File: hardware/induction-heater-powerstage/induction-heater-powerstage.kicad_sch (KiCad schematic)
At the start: 17 parts, among them IC1 MAX17601ASA+, J2 Screw_Terminal_01x02, J3 Screw_Terminal_01x01, J4 Screw_Terminal_01x01, J5 Screw_Terminal_01x01, J6 Screw_Terminal_01x01, J7 RJ12, Q1 NTH4L040N120M3S, Q3 NTH4L040N120M3S

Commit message: Fixed the mosfet driver grounds
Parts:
- removed JP1: SolderJumper_2_Open, Jumper:SolderJumper-2_P1.3mm_Open_TrianglePad1.0x1.5mm, symbol Jumper:SolderJumper_2_Open
- added NT1: NetTie_2, NetTie:NetTie-2_SMD_Pad2.0mm, symbol Device:NetTie_2
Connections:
- net GND: now also C1.2, J7.3, J7.5, NT1.2
- net GND2: now also NT1.1; no longer C1.2, J7.3, J7.5
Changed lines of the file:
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@@
 (kicad_sch (version 20230121) (generator eeschema)
   (paper "A4")
+  (junction (at 185.42 104.14) (diameter 0) (color 0 0 0 0)
+  )
   (junction (at 101.6 114.3) (diameter 0) (color 0 0 0 0)
   )
-  (junction (at 190.5 104.14) (diameter 0) (color 0 0 0 0)
-  )
   (junction (at 101.6 82.55) (diameter 0) (color 0 0 0 0)
   )
@@
   (junction (at 101.6 97.79) (diameter 0) (color 0 0 0 0)
   )
-  (junction (at 190.5 109.22) (diameter 0) (color 0 0 0 0)
+  (junction (at 196.85 104.14) (diameter 0) (color 0 0 0 0)
   )
   (junction (at 180.34 76.2) (diameter 0) (color 0 0 0 0)
@@
     (stroke (width 0) (type default))
   )
-  (wire (pts (xy 200.66 99.06) (xy 190.5 99.06))
+  (wire (pts (xy 200.66 99.06) (xy 196.85 99.06))
     (stroke (width 0) (type default))
   )
@@
     (stroke (width 0) (type default))
   )
-  (wire (pts (xy 196.85 109.22) (xy 190.5 109.22))
-    (stroke (width 0) (type default))
-  )
   (wire (pts (xy 133.35 130.81) (xy 133.35 139.7))
     (stroke (width 0) (type default))
@@
     (stroke (width 0) (type default))
   )
+  (wire (pts (xy 196.85 104.14) (xy 196.85 114.3))
+    (stroke (width 0) (type default))
+  )
   (wire (pts (xy 154.94 101.6) (xy 142.24 101.6))
     (stroke (width 0) (type default))
@@
     (stroke (width 0) (type default))
   )
+  (wire (pts (xy 193.04 104.14) (xy 196.85 104.14))
+    (stroke (width 0) (type default))
+  )
   (wire (pts (xy 125.73 130.81) (xy 133.35 130.81))
     (stroke (width 0) (type default))
@@
     (stroke (width 0) (type default))
   )
-  (wire (pts (xy 196.85 118.11) (xy 196.85 119.38))
-    (stroke (width 0) (type default))
-  )
   (wire (pts (xy 95.25 100.33) (xy 95.25 104.14))
     (stroke (width 0) (type default))
@@
     (stroke (width 0) (type default))
   )
-  (wire (pts (xy 196.85 110.49) (xy 196.85 109.22))
-    (stroke (width 0) (type default))
-  )
   (wire (pts (xy 133.35 91.44) (xy 133.35 101.6))
     (stroke (width 0) (type default))
   )
-  (wire (pts (xy 190.5 99.06) (xy 190.5 104.14))
+  (wire (pts (xy 196.85 99.06) (xy 196.85 104.14))
     (stroke (width 0) (type default))
   )
@@
     (stroke (width 0) (type default))
   )
-  (wire (pts (xy 190.5 104.14) (xy 190.5 109.22))
-    (stroke (width 0) (type default))
-  )
   (wire (pts (xy 154.94 106.68) (xy 142.24 106.68))
     (stroke (width 0) (type default))
@@
     (stroke (width 0) (type default))
   )
-  (wire (pts (xy 182.88 104.14) (xy 190.5 104.14))
+  (wire (pts (xy 182.88 104.14) (xy 185.42 104.14))
     (stroke (width 0) (type default))
   )
@@
     (stroke (width 0) (type default))
   )
+  (wire (pts (xy 185.42 104.14) (xy 185.42 114.3))
+    (stroke (width 0) (type default))
+  )
   (wire (pts (xy 125.73 91.44) (xy 133.35 91.44))
     (stroke (width 0) (type default))
@@
     (stroke (width 0) (type default))
   )
-  (wire (pts (xy 190.5 109.22) (xy 190.5 119.38))
-    (stroke (width 0) (type default))
-  )
   (wire (pts (xy 175.26 76.2) (xy 180.34 76.2))
     (stroke (width 0) (type default))
   )
+  (wire (pts (xy 185.42 104.14) (xy 187.96 104.14))
+    (stroke (width 0) (type default))
+  )
+  (wire (pts (xy 196.85 104.14) (xy 200.66 104.14))
+    (stroke (width 0) (type default))
+  )
   (wire (pts (xy 101.6 109.22) (xy 101.6 114.3))
     (stroke (width 0) (type default))
@@
   )
   (wire (pts (xy 101.6 114.3) (xy 118.11 114.3))
-    (stroke (width 0) (type default))
-  )
-  (wire (pts (xy 190.5 104.14) (xy 200.66 104.14))
     (stroke (width 0) (type default))
   )
@@
     )
   )
-  (symbol (lib_id "power:GND2") (at 190.5 119.38 0) (unit 1)
-    (in_bom yes) (on_board yes) (dnp no) (fields_autoplaced)
-    (property "Reference" "#PWR07" (at 190.5 125.73 0)
-      (effects (font (size 1.27 1.27)) hide)
-    )
-    (property "Value" "GND2" (at 190.5 124.46 0)
-      (effects (font (size 1.27 1.27)))
-    )
-    (property "Footprint" "" (at 190.5 119.38 0)
-      (effects (font (size 1.27 1.27)) hide)
-    )
-    (property "Datasheet" "" (at 190.5 119.38 0)
+  (symbol (lib_id "power:GND2") (at 185.42 114.3 0) (unit 1)
+    (in_bom yes) (on_board yes) (dnp no) (fields_autoplaced)
+    (property "Reference" "#PWR07" (at 185.42 120.65 0)
+      (effects (font (size 1.27 1.27)) hide)
+    )
+    (property "Value" "GND2" (at 185.42 119.38 0)
+      (effects (font (size 1.27 1.27)))
+    )
+    (property "Footprint" "" (at 185.42 114.3 0)
+      (effects (font (size 1.27 1.27)) hide)
+    )
+    (property "Datasheet" "" (at 185.42 114.3 0)
       (effects (font (size 1.27 1.27)) hide)
     )
@@
         (path "/cd13bc0f-8ba2-41f2-9e37-856c295399b9"
           (reference "L1") (unit 1)
+        )
+      )
+    )
+  )
+  (symbol (lib_id "power:GND") (at 196.85 114.3 0) (unit 1)
+    (in_bom yes) (on_board yes) (dnp no) (fields_autoplaced)
+    (property "Reference" "#PWR010" (at 196.85 120.65 0)
+      (effects (font (size 1.27 1.27)) hide)
+    )
+    (property "Value" "GND" (at 196.85 119.38 0)
+      (effects (font (size 1.27 1.27)))
+    )
+    (property "Footprint" "" (at 196.85 114.3 0)
+      (effects (font (size 1.27 1.27)) hide)
+    )
+    (property "Datasheet" "" (at 196.85 114.3 0)
+      (effects (font (size 1.27 1.27)) hide)
+    )
+    (pin "1")
+    (instances
+      (project "induction-heater-powerstage"
+        (path "/27d95e22-9cd6-4512-b5aa-6a1ddb34ce7c"
+          (reference "#PWR010") (unit 1)
         )
       )
@@
         (path "/27d95e22-9cd6-4512-b5aa-6a1ddb34ce7c"
           (reference "#PWR03") (unit 1)
-        )
-      )
-    )
-  )
-  (symbol (lib_id "power:GND") (at 196.85 119.38 0) (unit 1)
-    (in_bom yes) (on_board yes) (dnp no) (fields_autoplaced)
-    (property "Reference" "#PWR09" (at 196.85 125.73 0)
-      (effects (font (size 1.27 1.27)) hide)
-    )
-    (property "Value" "GND" (at 196.85 124.46 0)
-      (effects (font (size 1.27 1.27)))
-    )
-    (property "Footprint" "" (at 196.85 119.38 0)
-      (effects (font (size 1.27 1.27)) hide)
-    )
-    (property "Datasheet" "" (at 196.85 119.38 0)
-      (effects (font (size 1.27 1.27)) hide)
-    )
-    (pin "1")
-    (instances
-      (project "induction-heater-powerstage"
-        (path "/27d95e22-9cd6-4512-b5aa-6a1ddb34ce7c"
-          (reference "#PWR09") (unit 1)
-        )
-      )
-    )
-  )
-  (symbol (lib_id "power:GND2") (at 152.4 119.38 0) (unit 1)
-    (in_bom yes) (on_board yes) (dnp no) (fields_autoplaced)
-    (property "Reference" "#PWR04" (at 152.4 125.73 0)
-      (effects (font (size 1.27 1.27)) hide)
-    )
-    (property "Value" "GND2" (at 152.4 124.46 0)
-      (effects (font (size 1.27 1.27)))
-    )
-    (property "Footprint" "" (at 152.4 119.38 0)
-      (effects (font (size 1.27 1.27)) hide)
-    )
-    (property "Datasheet" "" (at 152.4 119.38 0)
-      (effects (font (size 1.27 1.27)) hide)
-    )
-    (pin "1")
-    (instances
-      (project "induction-heater-powerstage"
-        (path "/27d95e22-9cd6-4512-b5aa-6a1ddb34ce7c"
-          (reference "#PWR04") (unit 1)
         )
       )
@@
     )
   )
+  (symbol (lib_id "power:GND") (at 152.4 119.38 0) (unit 1)
+    (in_bom yes) (on_board yes) (dnp no) (fields_autoplaced)
+    (property "Reference" "#PWR04" (at 152.4 125.73 0)
+      (effects (font (size 1.27 1.27)) hide)
+    )
+    (property "Value" "GND" (at 152.4 124.46 0)
+      (effects (font (size 1.27 1.27)))
+    )
+    (property "Footprint" "" (at 152.4 119.38 0)
+      (effects (font (size 1.27 1.27)) hide)
+    )
+    (property "Datasheet" "" (at 152.4 119.38 0)
+      (effects (font (size 1.27 1.27)) hide)
+    )
+    (pin "1")
+    (instances
+      (project "induction-heater-powerstage"
+        (path "/27d95e22-9cd6-4512-b5aa-6a1ddb34ce7c"
+          (reference "#PWR04") (unit 1)
+        )
+      )
+    )
+  )
   (symbol (lib_id "Connector:Screw_Terminal_01x01") (at 118.11 120.65 270) (unit 1)
     (in_bom yes) (on_board yes) (dnp no) (fields_autoplaced)
@@
     )
   )
-  (symbol (lib_id "Jumper:SolderJumper_2_Open") (at 196.85 114.3 90) (unit 1)
-    (in_bom yes) (on_board yes) (dnp no) (fields_autoplaced)
-    (property "Reference" "JP1" (at 199.39 113.03 90)
-      (effects (font (size 1.27 1.27)) (justify right))
-    )
-    (property "Value" "SolderJumper_2_Open" (at 199.39 115.57 90)
-      (effects (font (size 1.27 1.27)) (justify right))
-    )
-    (property "Footprint" "Jumper:SolderJumper-2_P1.3mm_Open_TrianglePad1.0x1.5mm" (at 196.85 114.3 0)
-      (effects (font (size 1.27 1.27)) hide)
-    )
-    (property "Datasheet" "~" (at 196.85 114.3 0)
-      (effects (font (size 1.27 1.27)) hide)
-    )
-    (pin "1")
-    (pin "2")
-    (instances
-      (project "induction-heater-powerstage"
-        (path "/27d95e22-9cd6-4512-b5aa-6a1ddb34ce7c"
-          (reference "JP1") (unit 1)
-        )
-      )
-      (project "induction-heater-controller"
-        (path "/339ad394-821c-4472-87df-af0d8e6d98cf"
-          (reference "JP1") (unit 1)
-        )
-      )
+  (symbol (lib_id "Device:NetTie_2") (at 190.5 104.14 0) (unit 1)
+    (in_bom no) (on_board yes) (dnp no) (fields_autoplaced)
+    (property "Reference" "NT1" (at 190.5 99.06 0)
+      (effects (font (size 1.27 1.27)))
+    )
+    (property "Value" "NetTie_2" (at 190.5 101.6 0)
+      (effects (font (size 1.27 1.27)))
+    )
+    (property "Footprint" "NetTie:NetTie-2_SMD_Pad2.0mm" (at 190.5 104.14 0)
+      (effects (font (size 1.27 1.27)) hide)
+    )
+    (property "Datasheet" "~" (at 190.5 104.14 0)
+      (effects (font (size 1.27 1.27)) hide)
+    )
+    (pin "1")
+    (pin "2")
+    (instances
+      (project "induction-heater-powerstage"
+        (path "/27d95e22-9cd6-4512-b5aa-6a1ddb34ce7c"
+          (reference "NT1") (unit 1)
+        )
+      )

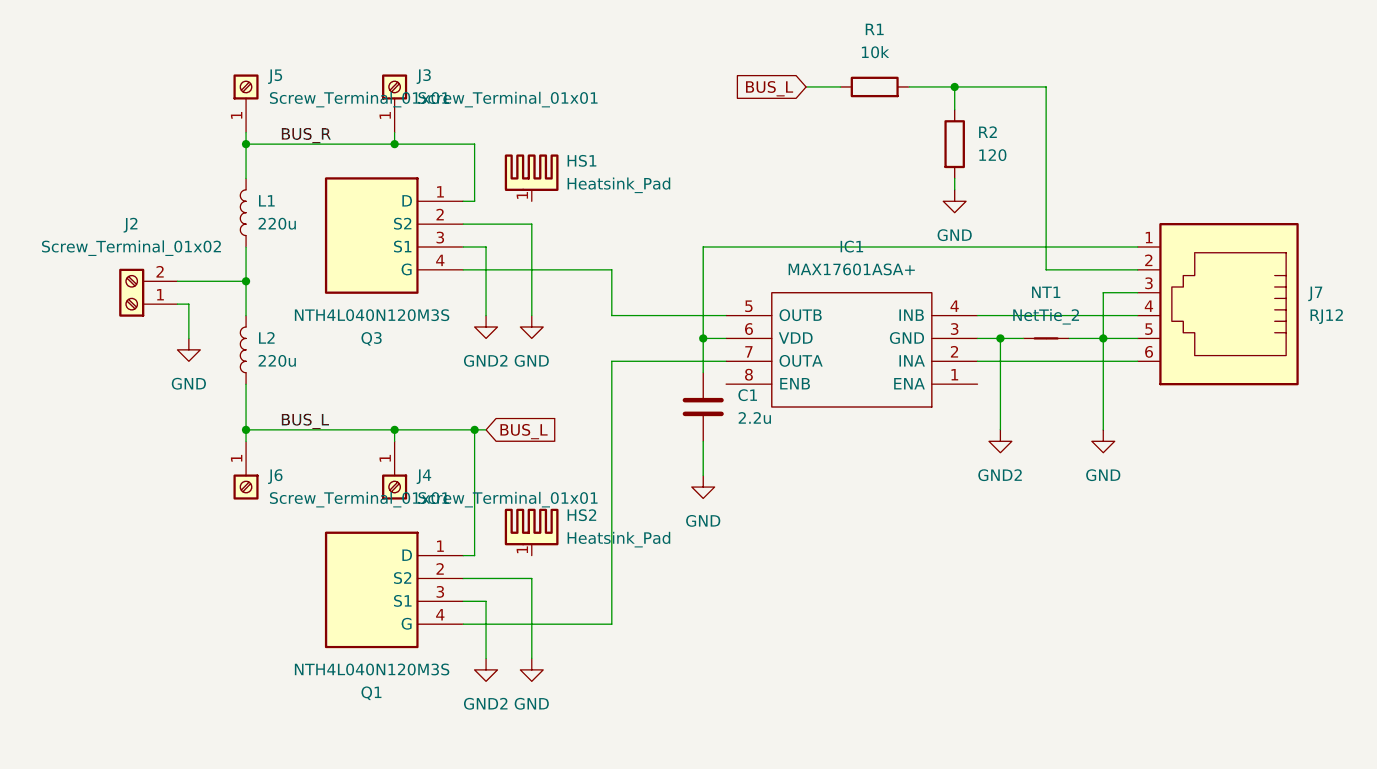
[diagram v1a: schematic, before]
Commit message: Move to IGBTs
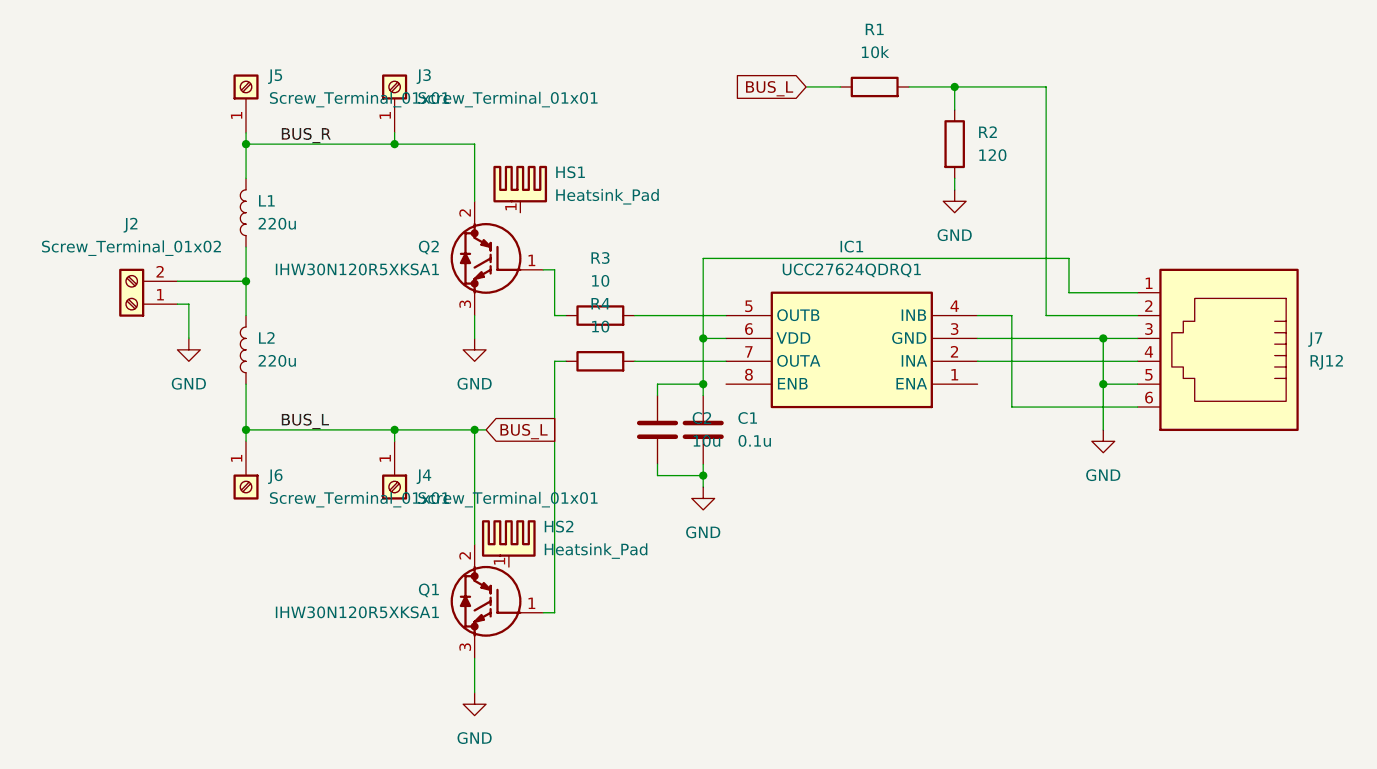
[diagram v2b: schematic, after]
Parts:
- removed IC1: MAX17601ASA+, SOIC127P600X175-8N, symbol custom:MAX17601ASA+
- removed NT1: NetTie_2, NetTie:NetTie-2_SMD_Pad2.0mm, symbol Device:NetTie_2
- removed Q1, Q3: NTH4L040N120M3S, NTH4L040N120M3S, symbol custom:NTH4L040N120M3S
- added C2: 10u, Capacitor_SMD:C_0805_2012Metric_Pad1.18x1.45mm_HandSolder, symbol Device:C
- added IC1: UCC27624QDRQ1, SOIC127P600X175-8N, symbol custom:UCC27624QDRQ1
- added Q1, Q2: IHW30N120R5XKSA1, TO544P521X1592X2557-3P, symbol custom:IHW30N120R5XKSA1
- added R3, R4: 10, Resistor_SMD:R_0805_2012Metric_Pad1.20x1.40mm_HandSolder, symbol Device:R
- C1: value 2.2u -> 0.1u; footprint Capacitor_SMD:C_0805_2012Metric -> Capacitor_SMD:C_0805_2012Metric_Pad1.18x1.45mm_HandSolder
- R1, R2: footprint Resistor_SMD:R_0805_2012Metric -> Resistor_SMD:R_0805_2012Metric_Pad1.20x1.40mm_HandSolder
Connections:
- net BUS_L: now also Q1.2 (C)
- net BUS_R: now also Q2.2 (C)
- net GND: now also C2.2, IC1.3 (GND), Q1.3 (E), Q2.3 (E)
- net at C1.1, J7.1: now also C2.1, IC1.6 (VDD)
- net at J7.4: now also IC1.2 (INA)
- net at J7.6: now also IC1.4 (INB)
- new net: Q2.1 (G), R3.1
- new net: IC1.5 (OUTB), R3.2
- new net: IC1.7 (OUTA), R4.2
- new net: Q1.1 (G), R4.1
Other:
- moved on the sheet: C1, HS1, HS2, J7

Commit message: Final components
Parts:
- C1: MPN (none) -> CL21B104KCFSFNG
- C2: MPN (none) -> CL21A106KAYNNNG
- HS1, HS2: MPN 6398BG -> 6400BG
- IC1: MPN (none) -> UCC27624QDRQ1
- Q1, Q2: MPN (none) -> IHW30N120R5XKSA1
- R1: MPN (none) -> RC0805JR-1010KL
- R2: MPN (none) -> RC0805FR-07120RL
- R3, R4: MPN (none) -> RC0805FR-1010RL
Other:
- moved on the sheet: R3, R4
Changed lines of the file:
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@@
     (stroke (width 0) (type default))
   )
-  (wire (pts (xy 137.16 101.6) (xy 135.89 101.6))
+  (wire (pts (xy 140.97 101.6) (xy 138.43 101.6))
     (stroke (width 0) (type default))
   )
@@
     (stroke (width 0) (type default))
   )
-  (wire (pts (xy 135.89 106.68) (xy 135.89 134.62))
+  (wire (pts (xy 138.43 106.68) (xy 138.43 134.62))
     (stroke (width 0) (type default))
   )
@@
     (stroke (width 0) (type default))
   )
-  (wire (pts (xy 134.62 96.52) (xy 135.89 96.52))
-    (stroke (width 0) (type default))
-  )
-  (wire (pts (xy 154.94 101.6) (xy 144.78 101.6))
+  (wire (pts (xy 134.62 96.52) (xy 138.43 96.52))
+    (stroke (width 0) (type default))
+  )
+  (wire (pts (xy 154.94 101.6) (xy 148.59 101.6))
     (stroke (width 0) (type default))
   )
@@
     (stroke (width 0) (type default))
   )
-  (wire (pts (xy 135.89 96.52) (xy 135.89 101.6))
+  (wire (pts (xy 138.43 96.52) (xy 138.43 101.6))
     (stroke (width 0) (type default))
   )
@@
     (stroke (width 0) (type default))
   )
-  (wire (pts (xy 154.94 106.68) (xy 144.78 106.68))
+  (wire (pts (xy 154.94 106.68) (xy 148.59 106.68))
     (stroke (width 0) (type default))
   )
@@
     (stroke (width 0) (type default))
   )
-  (wire (pts (xy 137.16 106.68) (xy 135.89 106.68))
+  (wire (pts (xy 140.97 106.68) (xy 138.43 106.68))
     (stroke (width 0) (type default))
   )
@@
     (stroke (width 0) (type default))
   )
-  (wire (pts (xy 134.62 134.62) (xy 135.89 134.62))
+  (wire (pts (xy 134.62 134.62) (xy 138.43 134.62))
     (stroke (width 0) (type default))
   )
@@
   )
   (symbol (lib_id "Device:C") (at 147.32 114.3 0) (unit 1)
-    (in_bom yes) (on_board yes) (dnp no) (fields_autoplaced)
-    (property "Reference" "C2" (at 151.13 113.03 0)
-      (effects (font (size 1.27 1.27)) (justify left))
-    )
-    (property "Value" "10u" (at 151.13 115.57 0)
+    (in_bom yes) (on_board yes) (dnp no)
+    (property "Reference" "C2" (at 140.97 113.03 0)
+      (effects (font (size 1.27 1.27)) (justify left))
+    )
+    (property "Value" "10u" (at 140.97 115.57 0)
       (effects (font (size 1.27 1.27)) (justify left))
     )
@@
       (effects (font (size 1.27 1.27)) hide)
     )
+    (property "MPN" "CL21A106KAYNNNG" (at 147.32 114.3 0)
+      (effects (font (size 1.27 1.27)) hide)
+    )
     (pin "1")
     (pin "2")
@@
       (effects (font (size 1.27 1.27)) hide)
     )
+    (property "MPN" "RC0805JR-1010KL" (at 171.45 76.2 90)
+      (effects (font (size 1.27 1.27)) hide)
+    )
     (pin "1")
     (pin "2")
@@
     )
     (property "Datasheet" "~" (at 180.34 82.55 0)
+      (effects (font (size 1.27 1.27)) hide)
+    )
+    (property "MPN" "RC0805FR-07120RL" (at 180.34 82.55 0)
       (effects (font (size 1.27 1.27)) hide)
     )
@@
       (effects (font (size 1.27 1.27)) (justify left top) hide)
     )
+    (property "MPN" "IHW30N120R5XKSA1" (at 134.62 96.52 0)
+      (effects (font (size 1.27 1.27)) hide)
+    )
     (pin "1")
     (pin "2")
@@
     (property "Manufacturer_Part_Number" "UCC27624QDRQ1" (at 158.75 -685.7 0)
       (effects (font (size 1.27 1.27)) (justify left top) hide)
+    )
+    (property "MPN" "UCC27624QDRQ1" (at 182.88 109.22 0)
+      (effects (font (size 1.27 1.27)) hide)
     )
     (pin "1")
@@
       (effects (font (size 1.27 1.27)) hide)
     )
+    (property "MPN" "CL21B104KCFSFNG" (at 152.4 114.3 0)
+      (effects (font (size 1.27 1.27)) hide)
+    )
     (pin "1")
     (pin "2")
@@
     )
   )
-  (symbol (lib_id "Device:R") (at 140.97 101.6 90) (unit 1)
-    (in_bom yes) (on_board yes) (dnp no) (fields_autoplaced)
-    (property "Reference" "R3" (at 140.97 95.25 90)
-      (effects (font (size 1.27 1.27)))
-    )
-    (property "Value" "10" (at 140.97 97.79 90)
-      (effects (font (size 1.27 1.27)))
-    )
-    (property "Footprint" "Resistor_SMD:R_0805_2012Metric_Pad1.20x1.40mm_HandSolder" (at 140.97 103.378 90)
-      (effects (font (size 1.27 1.27)) hide)
-    )
-    (property "Datasheet" "~" (at 140.97 101.6 0)
+  (symbol (lib_id "Device:R") (at 144.78 101.6 90) (unit 1)
+    (in_bom yes) (on_board yes) (dnp no)
+    (property "Reference" "R3" (at 144.78 99.06 90)
+      (effects (font (size 1.27 1.27)))
+    )
+    (property "Value" "10" (at 144.78 101.6 90)
+      (effects (font (size 1.27 1.27)))
+    )
+    (property "Footprint" "Resistor_SMD:R_0805_2012Metric_Pad1.20x1.40mm_HandSolder" (at 144.78 103.378 90)
+      (effects (font (size 1.27 1.27)) hide)
+    )
+    (property "Datasheet" "~" (at 144.78 101.6 0)
+      (effects (font (size 1.27 1.27)) hide)
+    )
+    (property "MPN" "RC0805FR-1010RL" (at 144.78 101.6 90)
       (effects (font (size 1.27 1.27)) hide)
     )
@@
       (effects (font (size 1.27 1.27)) hide)
     )
-    (property "MPN" "6398BG" (at 130.81 127 0)
+    (property "MPN" "6400BG" (at 130.81 127 0)
       (effects (font (size 1.27 1.27)) hide)
     )
@@
       (effects (font (size 1.27 1.27)) (justify left top) hide)
     )
+    (property "MPN" "IHW30N120R5XKSA1" (at 134.62 134.62 0)
+      (effects (font (size 1.27 1.27)) hide)
+    )
     (pin "1")
     (pin "2")
@@
     )
   )
-  (symbol (lib_id "Device:R") (at 140.97 106.68 90) (unit 1)
-    (in_bom yes) (on_board yes) (dnp no) (fields_autoplaced)
-    (property "Reference" "R4" (at 140.97 100.33 90)
-      (effects (font (size 1.27 1.27)))
-    )
-    (property "Value" "10" (at 140.97 102.87 90)
-      (effects (font (size 1.27 1.27)))
-    )
-    (property "Footprint" "Resistor_SMD:R_0805_2012Metric_Pad1.20x1.40mm_HandSolder" (at 140.97 108.458 90)
-      (effects (font (size 1.27 1.27)) hide)
-    )
-    (property "Datasheet" "~" (at 140.97 106.68 0)
+  (symbol (lib_id "Device:R") (at 144.78 106.68 90) (unit 1)
+    (in_bom yes) (on_board yes) (dnp no)
+    (property "Reference" "R4" (at 144.78 104.14 90)
+      (effects (font (size 1.27 1.27)))
+    )
+    (property "Value" "10" (at 144.78 106.68 90)
+      (effects (font (size 1.27 1.27)))
+    )
+    (property "Footprint" "Resistor_SMD:R_0805_2012Metric_Pad1.20x1.40mm_HandSolder" (at 144.78 108.458 90)
+      (effects (font (size 1.27 1.27)) hide)
+    )
+    (property "Datasheet" "~" (at 144.78 106.68 0)
+      (effects (font (size 1.27 1.27)) hide)
+    )
+    (property "MPN" "RC0805FR-1010RL" (at 144.78 106.68 90)
       (effects (font (size 1.27 1.27)) hide)
     )
@@
       (effects (font (size 1.27 1.27)) hide)
     )
-    (property "MPN" "6398BG" (at 132.08 87.63 0)
-      (effects (font (size 1.27 1.27)) hide)
-    )
+    (property "MPN" "6400BG" (at 132.08 87.63 0)
+      (effects (font (size 1.27 1.27)) hide)
+    )
